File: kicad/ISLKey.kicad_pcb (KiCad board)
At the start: 2 copper layers, 140.9 x 132 mm, 46 parts, among them J10 5-60V AC/DC IN, J11 12V OUT (lock/aux), J13 TTGO batt pads, J3 Exit btn, J4 Door contact, J5 Tamper, J6 LOCK COM/NO/NC, J7 AUX COM/NO/NC, J8 Fire volt-free, J9 Fire link COM-Fire, K1 SRD-05VDC-SL-C, K2 SRD-05VDC-SL-C, M1 TTGO T-Display, Q1 PN2222A, Q2 PN2222A, U1 PC817, U3 TEN20-2412WIN, U4 TSR-1-2450, U5 DS3231M

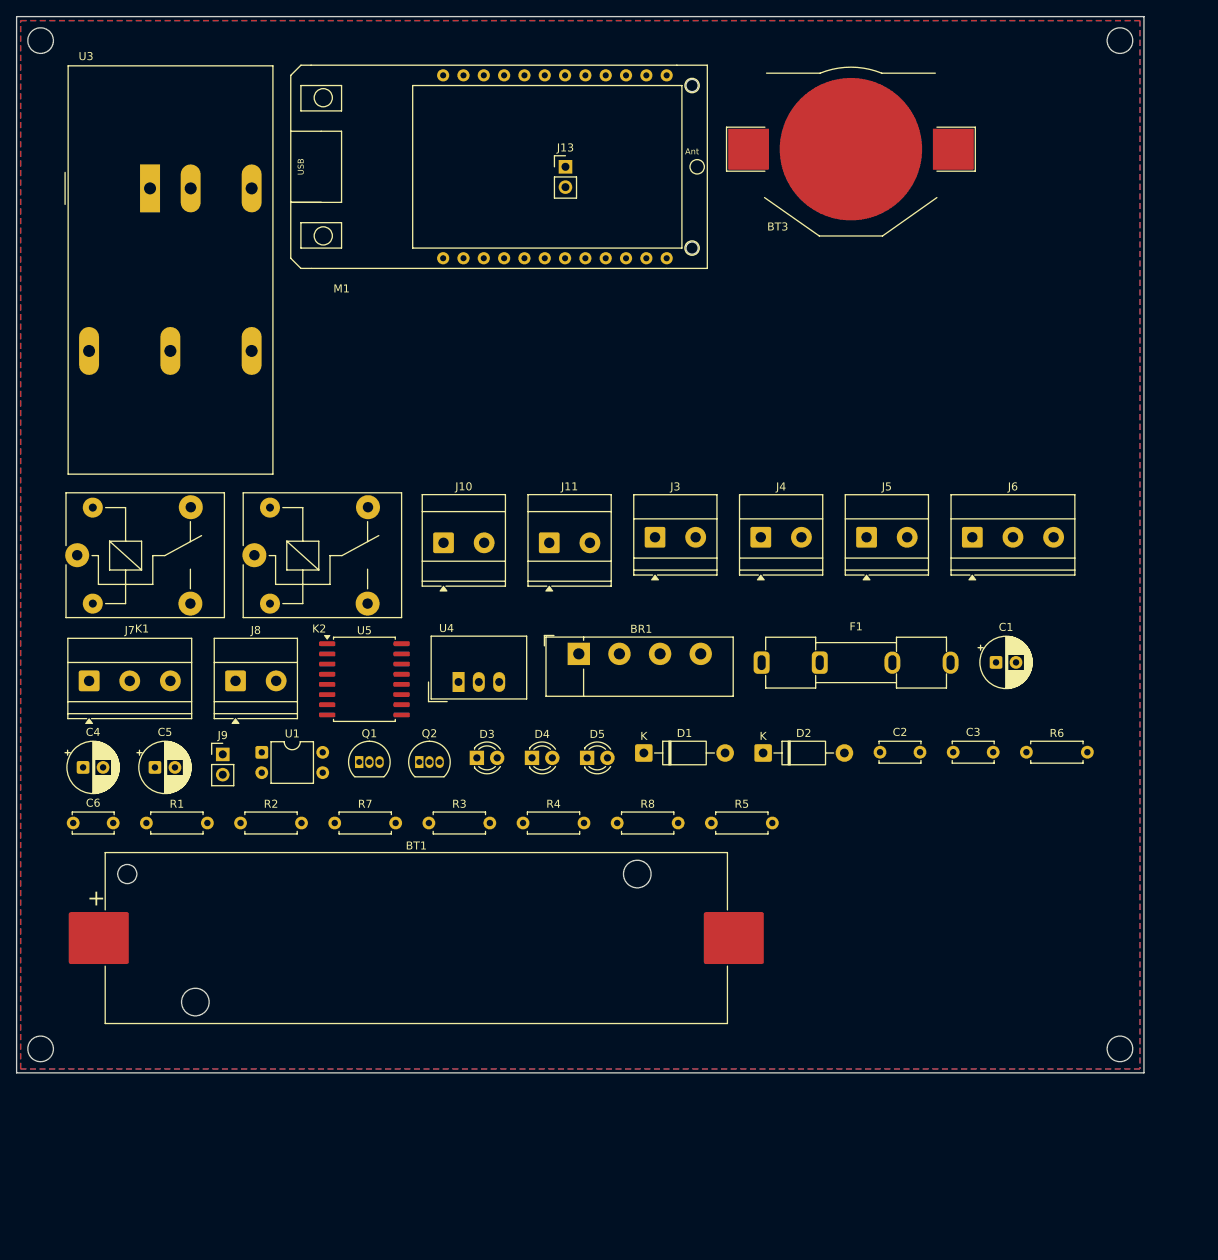
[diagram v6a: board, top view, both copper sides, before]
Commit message: kicad: autoroute the board (Freerouting) -- 262 traces + 9 vias
Full copper route via Freerouting 2.2.4 (portable JRE25, headless batch):
export Specctra DSN -> autoroute -> import SES. Placement loosened to
GAP=4mm/W=140 (148x153mm) for routing channels; net classes trimmed to
Power 0.4mm / Lock 0.6mm so the wide nets fit. GND pour set to solid pad
connection on both layers.

Result: 62 nets routed, DRC clean bar cosmetic silk-height (imported TTGO
footprint) + one RTC (U5) ground pin needing a manual via in a congested
spot. Board-gen quirk noted in-code: ExportSpecctraDSN won't overwrite an
existing file -- delete first.

Co-Authored-By: Claude Opus 4.8 <noreply@anthropic.com>
Claude-Session: https://claude.ai/code/session_01WaJbCVpNNC7xF4fkqWpjpA
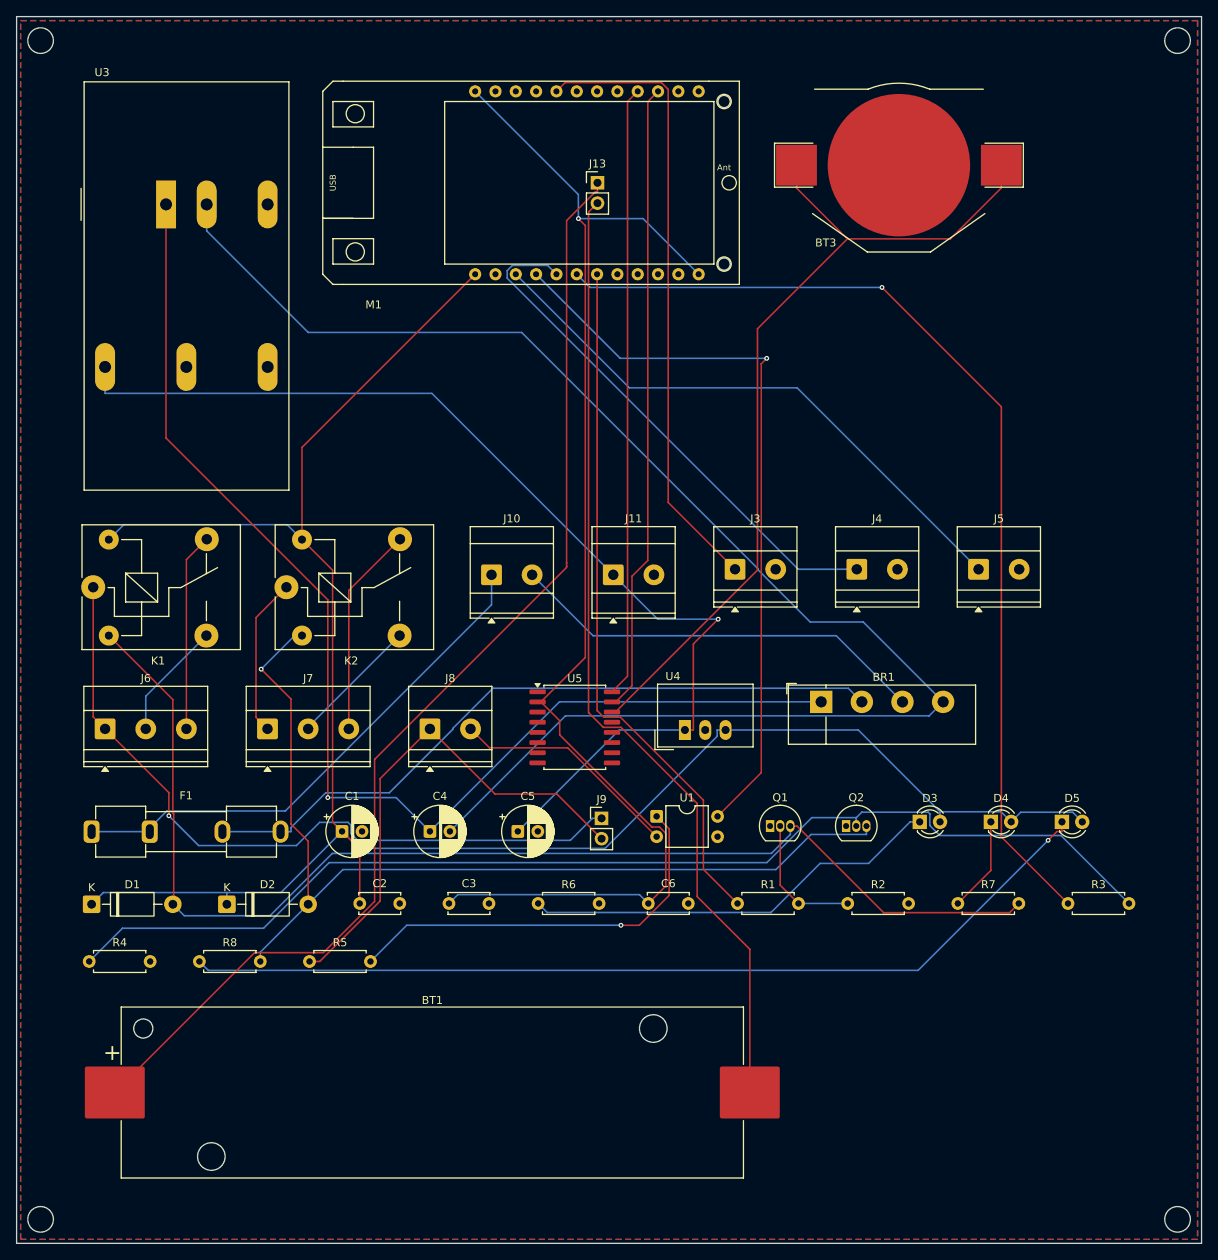
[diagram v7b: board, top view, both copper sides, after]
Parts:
- moved J6 111.0 mm to (11.1, 89.0)
- moved F1 86.4 mm to (9.38, 101.9)
- moved C1 84.4 mm to (40.7, 101.8)
- moved R3 80.5 mm to (131.4, 110.9)
- moved R7 78.5 mm to (117.7, 110.9)
- moved R2 76.6 mm to (103.9, 110.9)
- moved R1 74.6 mm to (90.1, 110.9)
- moved C6 72.6 mm to (79.0, 110.9)
- moved D1 71.6 mm to (9.38, 111.0)
- moved D2 69.6 mm to (26.3, 111.0)
- moved C2 67.7 mm to (42.9, 110.9)
- moved C3 65.8 mm to (54.0, 110.9)
- moved R6 63.9 mm to (65.2, 110.9)
- moved D5 59.9 mm to (130.7, 100.7)
- moved D4 57.9 mm to (121.8, 100.7)
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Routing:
- net +5V: track 0.00 -> 259.9 mm
- net PGND: track 0.00 -> 188.2 mm
- net +3V3: track 0.00 -> 161.6 mm, vias 0 -> 1
- net K1_C: track 0.00 -> 153.5 mm
- net RAWP: track 0.00 -> 152.7 mm, vias 0 -> 1
- net RLY2_B: track 0.00 -> 144.3 mm
- net VBAT: track 0.00 -> 143.9 mm
- net +12V: track 0.00 -> 134.0 mm, vias 0 -> 1
- net RLY2: track 0.00 -> 125.5 mm, vias 0 -> 1
- net K2_C: track 0.00 -> 122.7 mm, vias 0 -> 1
- net GND_BAT: track 0.00 -> 121.3 mm
- net D5K: track 0.00 -> 116.7 mm, vias 0 -> 1
- net RTC_VBAT: track 0.00 -> 108.2 mm
- net FIRE_SENSE: track 0.00 -> 93.0 mm, vias 0 -> 1
- net LK1_COM: track 0.00 -> 92.0 mm, vias 0 -> 1
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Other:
- board size 140.9 x 132 mm -> 148.1 x 153.3 mm

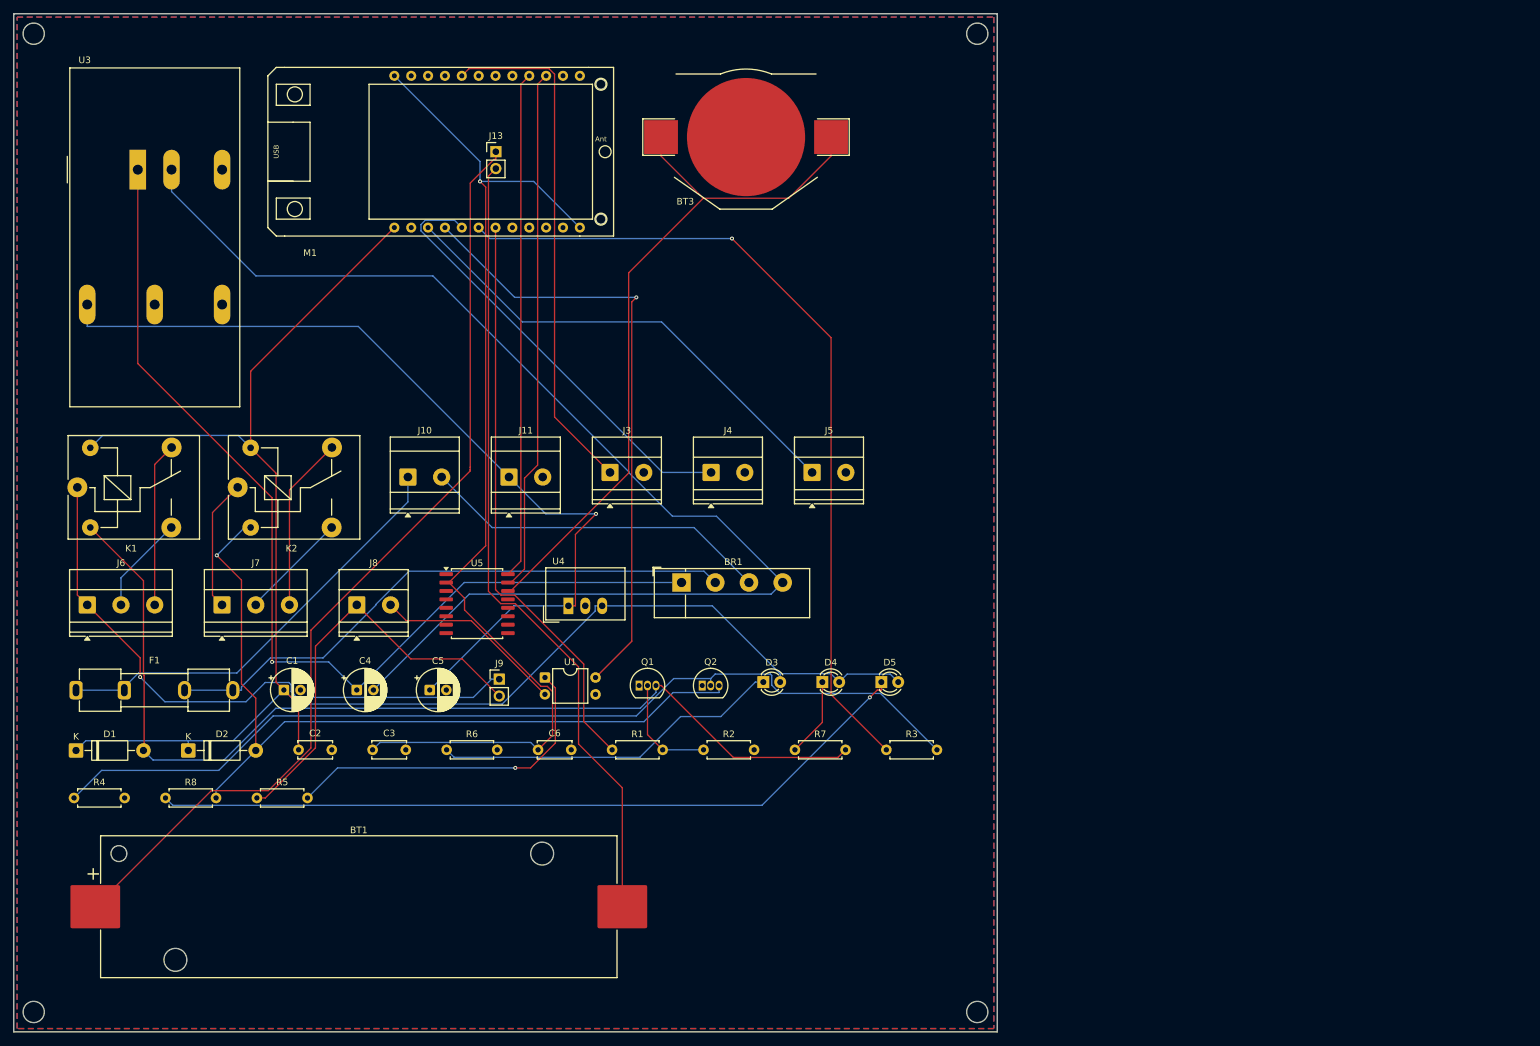
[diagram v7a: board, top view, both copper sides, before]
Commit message: kicad: SMD passives, perimeter terminals, fully routed on user's placement
- Passives -> SMD (assembly-house placeable): R/LED 0805, ceramics 0805,
  flyback diodes SMA, electrolytics SMD alu (100V bulk on 10mm can).
- Fixed the Traco TEN20 footprint's buggy 51mm courtyard -> local
  lib/ISLKey.pretty/TEN20_TRACO (~26mm).
- User hand-placed the board in KiCad (terminals on the perimeter, USB-C
  clear, ~1/3 smaller). Repaired the malformed outline into a clean rect
  enclosing the corner mounting holes (148x128mm), redrew GND pours.
- Routed with Freerouting exporting the DSN WITHOUT the pour so GND routes
  as traces (avoids isolated pour-island unconnects): 368 traces + 22 vias,
  0 unrouted. DRC clean bar cosmetic silk-over-copper + text-height.

NOTE: ISLKey.kicad_pcb is now hand-placed + routed; do NOT re-run make_pcb.py
(it regenerates placement from scratch and would wipe this).

Co-Authored-By: Claude Opus 4.8 <noreply@anthropic.com>
Claude-Session: https://claude.ai/code/session_01WaJbCVpNNC7xF4fkqWpjpA
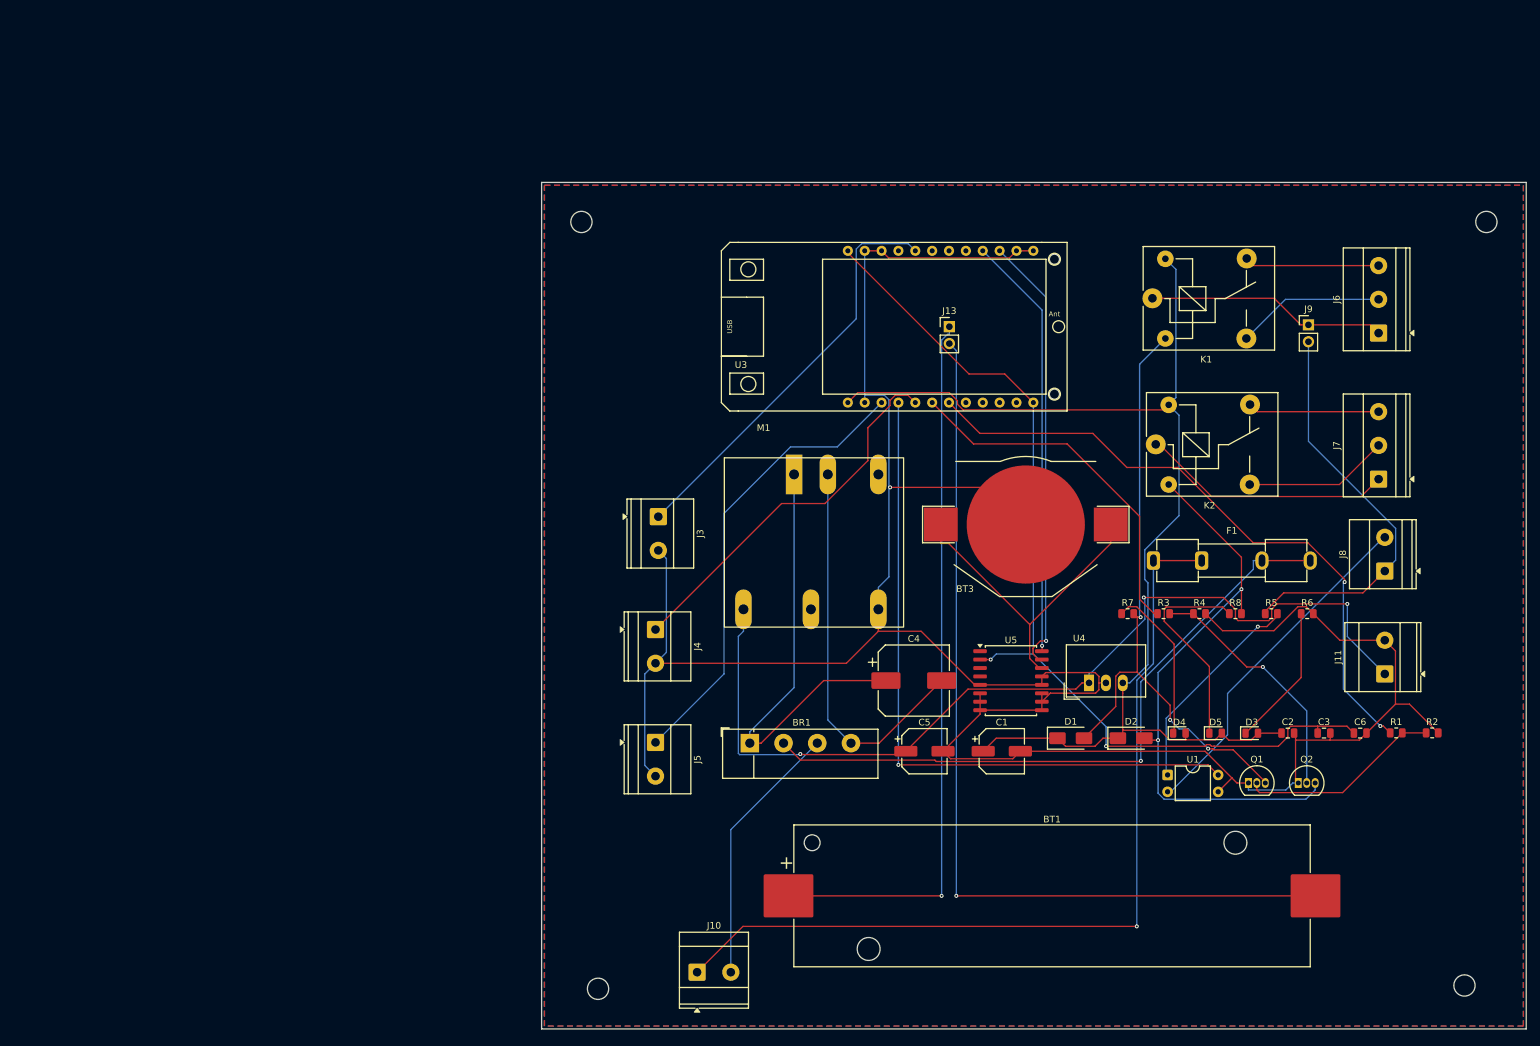
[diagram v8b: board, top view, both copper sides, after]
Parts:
- C1, C5: footprint CP_Radial_D6.3mm_P2.50mm -> CP_Elec_6.3x5.3
- C2, C3, C6: footprint C_Disc_D5.0mm_W2.5mm_P5.00mm -> C_0805_2012Metric
- C4: footprint CP_Radial_D6.3mm_P2.50mm -> CP_Elec_10x10.5
- D1, D2: footprint D_DO-41_SOD81_P10.16mm_Horizontal -> D_SMA
- D3, D4, D5: footprint LED_D3.0mm -> LED_0805_2012Metric
- R1, R2, R3, R4, R5, R6, R7, R8: footprint R_Axial_DIN0207_L6.3mm_D2.5mm_P7.62mm_Horizontal -> R_0805_2012Metric
- U3: footprint Converter_DCDC_TRACO_TEN20-xxxx_THT -> TEN20_TRACO
- moved J6 198.8 mm to (205.6, 48.1), turned to 90 degrees
- moved J7 175.2 mm to (205.6, 70.1), turned to 90 degrees
- moved R4 171.8 mm to (178.6, 90.4)
- moved K1 164.4 mm to (171.5, 42.9)
- moved R8 163.5 mm to (184.0, 90.4)
- moved F1 163.4 mm to (171.7, 82.4)
- moved R5 155.3 mm to (189.4, 90.4)
- moved J8 154.9 mm to (206.5, 83.9), turned to 90 degrees
- moved D1 149.8 mm to (159.2, 109.1)
- moved C2 149.0 mm to (191.9, 108.3)
- moved C3 143.3 mm to (197.3, 108.3)
- moved D2 142.0 mm to (168.3, 109.1)
- moved K2 138.4 mm to (172.0, 64.9)
- moved J11 135.2 mm to (206.5, 99.4), turned to 90 degrees
- moved J9 133.1 mm to (195.0, 46.9)
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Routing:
- net GND: track 0.00 -> 394.6 mm, vias 0 -> 1
- net PGND: track 188.2 -> 59.5 mm
- net RLY2_B: track 144.3 -> 37.6 mm, vias 0 -> 1
- net RAWP: track 152.7 -> 67.6 mm, vias 1 -> 0
- net D5K: track 116.7 -> 31.9 mm, vias 1 -> 0
- net +5V: track 259.9 -> 178.3 mm
- net RLY2: track 125.5 -> 54.4 mm, vias 1 -> 0
- net ACL: track 65.7 -> 132.5 mm, vias 0 -> 1
- net RTC_VBAT: track 108.2 -> 49.0 mm
- net K1_C: track 153.5 -> 95.6 mm, vias 0 -> 3
- net LK1_COM: track 92.0 -> 36.2 mm, vias 1 -> 0
- net K2_C: track 122.7 -> 87.8 mm, vias 1 -> 2
- net VBAT: track 143.9 -> 109.4 mm, vias 0 -> 1
- net D3K: track 52.9 -> 21.5 mm
- net FIRE_B: track 28.8 -> 52.2 mm
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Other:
- board size 148.1 x 153.3 mm -> 148.3 x 127.5 mm
